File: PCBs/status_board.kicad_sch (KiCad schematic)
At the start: 19 parts, among them J1 Conn_01x03, J2 Conn_01x03, J3 Conn_01x02, J4 Conn_01x04, J5 Conn_01x04, J6 Conn_01x02, U1 XIAO-ESP32-S3-SMD

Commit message: Flipped voltage readout
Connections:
- net GND: now also J5.1 (Pin_1); no longer J5.4 (Pin_4)
- net at J1.3 (Pin_3), J2.3 (Pin_3), J4.3 (Pin_3)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: now also J5.2 (Pin_2); no longer J5.3 (Pin_3)
- net at U1.11 (D10): now also J5.3 (Pin_3); no longer J5.1 (Pin_1)
- net at U1.10 (D9): now also J5.4 (Pin_4); no longer J5.2 (Pin_2)
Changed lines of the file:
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@@
-	)
-	(junction
-		(at 157.48 107.95)
-		(diameter 0)
-		(color 0 0 0 0)
 	)
 	(junction
@@
 		(color 0 0 0 0)
 	)
+	(junction
+		(at 166.37 99.06)
+		(diameter 0)
+		(color 0 0 0 0)
+	)
 	(wire
 		(pts
@@
 	(wire
 		(pts
-			(xy 166.37 102.87) (xy 167.64 102.87)
-		)
-		(stroke
-			(width 0)
-			(type default)
-		)
-	)
-	(wire
-		(pts
 			(xy 116.84 107.95) (xy 128.27 107.95)
 		)
@@
 	(wire
 		(pts
-			(xy 171.45 99.06) (xy 184.15 99.06)
-		)
-		(stroke
-			(width 0)
-			(type default)
-		)
-	)
-	(wire
-		(pts
 			(xy 46.99 64.77) (xy 46.99 68.58)
 		)
@@
 	(wire
 		(pts
-			(xy 175.26 104.14) (xy 171.45 107.95)
-		)
-		(stroke
-			(width 0)
-			(type default)
-		)
-	)
-	(wire
-		(pts
-			(xy 157.48 107.95) (xy 171.45 107.95)
-		)
-		(stroke
-			(width 0)
-			(type default)
-		)
-	)
-	(wire
-		(pts
 			(xy 59.69 57.15) (xy 92.71 57.15)
 		)
@@
 	(wire
 		(pts
+			(xy 167.64 104.14) (xy 166.37 102.87)
+		)
+		(stroke
+			(width 0)
+			(type default)
+		)
+	)
+	(wire
+		(pts
 			(xy 128.27 107.95) (xy 128.27 111.76)
 		)
@@
 	(wire
 		(pts
-			(xy 166.37 106.68) (xy 168.91 106.68)
-		)
-		(stroke
-			(width 0)
-			(type default)
-		)
-	)
-	(wire
-		(pts
 			(xy 109.22 111.76) (xy 109.22 110.49)
 		)
@@
 	(wire
 		(pts
+			(xy 184.15 101.6) (xy 168.91 101.6)
+		)
+		(stroke
+			(width 0)
+			(type default)
+		)
+	)
+	(wire
+		(pts
 			(xy 83.82 64.77) (xy 83.82 67.31)
 		)
@@
 	(wire
 		(pts
+			(xy 166.37 106.68) (xy 184.15 106.68)
+		)
+		(stroke
+			(width 0)
+			(type default)
+		)
+	)
+	(wire
+		(pts
 			(xy 72.39 64.77) (xy 72.39 71.12)
 		)
@@
 	(wire
 		(pts
-			(xy 173.99 101.6) (xy 184.15 101.6)
-		)
-		(stroke
-			(width 0)
-			(type default)
-		)
-	)
-	(wire
-		(pts
-			(xy 168.91 106.68) (xy 173.99 101.6)
-		)
-		(stroke
-			(width 0)
-			(type default)
-		)
-	)
-	(wire
-		(pts
 			(xy 96.52 64.77) (xy 96.52 68.58)
 		)
@@
 	(wire
 		(pts
-			(xy 167.64 102.87) (xy 171.45 99.06)
+			(xy 168.91 101.6) (xy 166.37 99.06)
 		)
 		(stroke
@@
 	(wire
 		(pts
-			(xy 175.26 104.14) (xy 184.15 104.14)
+			(xy 184.15 104.14) (xy 167.64 104.14)
 		)
 		(stroke
@@
 	(symbol
 		(lib_id "power:GND")
-		(at 184.15 106.68 270)
+		(at 184.15 99.06 270)
 		(unit 1)
 		(body_style 1)
@@
 		(fields_autoplaced yes)
 		(property "Reference" "#PWR07"
-			(at 177.8 106.68 0)
+			(at 177.8 99.06 0)
 			(hide yes)
 			(show_name no)
@@
 		)
 		(property "Value" "GND"
-			(at 180.34 106.6799 90)
+			(at 180.34 99.0599 90)
 			(show_name no)
 			(do_not_autoplace no)
@@
 		)
 		(property "Footprint" ""
-			(at 184.15 106.68 0)
+			(at 184.15 99.06 0)
 			(hide yes)
 			(show_name no)
@@
 		)
 		(property "Datasheet" ""
-			(at 184.15 106.68 0)
+			(at 184.15 99.06 0)
 			(hide yes)
 			(show_name no)
@@
 		)
 		(property "Description" "Power symbol creates a global label with name \"GND\" , ground"
-			(at 184.15 106.68 0)
-			(hide yes)
-			(show_name no)
+			(at 184.15 99.06 0)
+			(hide yes)
+			(show_name no)

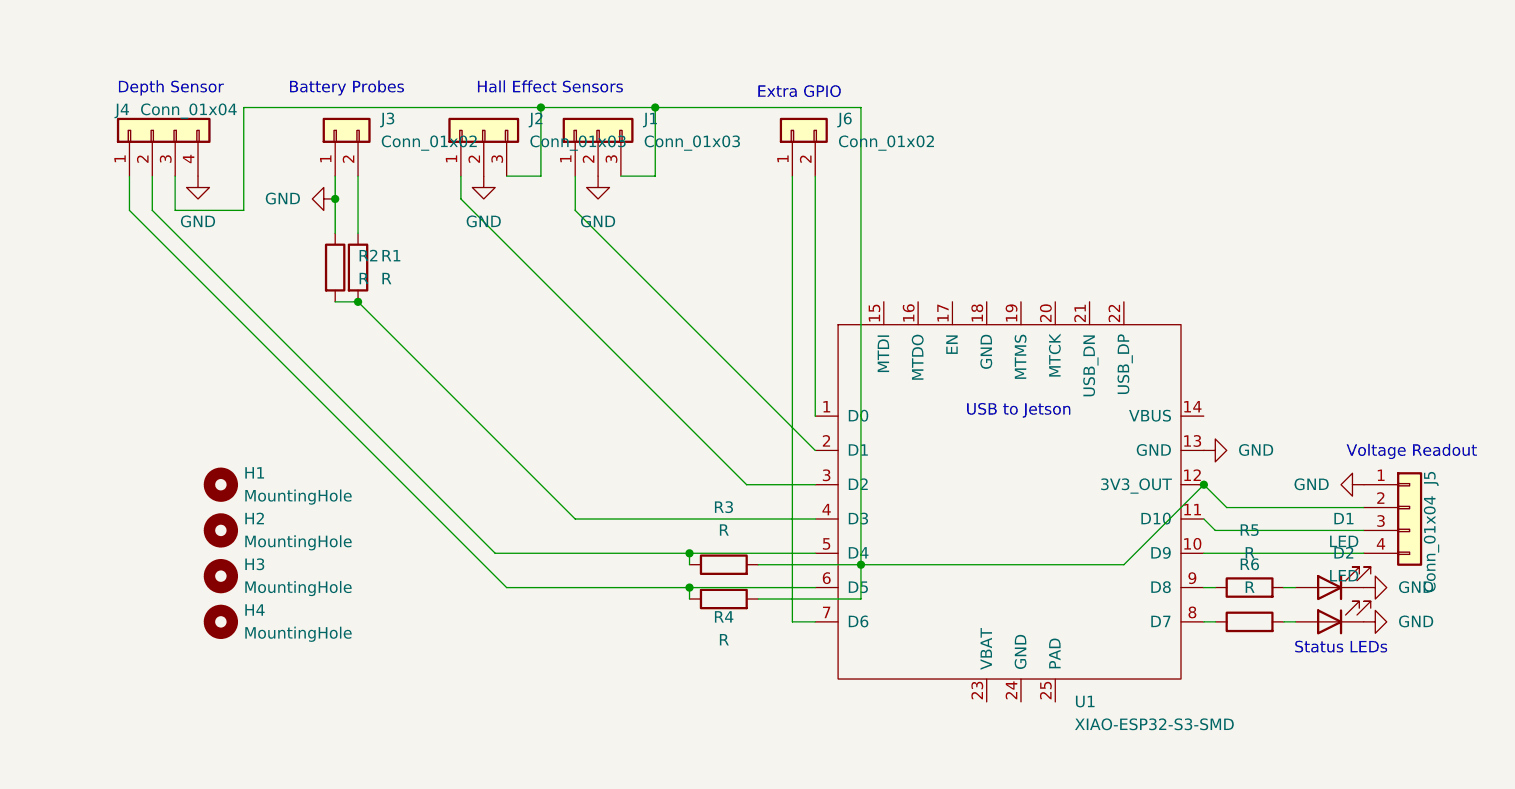
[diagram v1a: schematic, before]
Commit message: Removed connection crossover
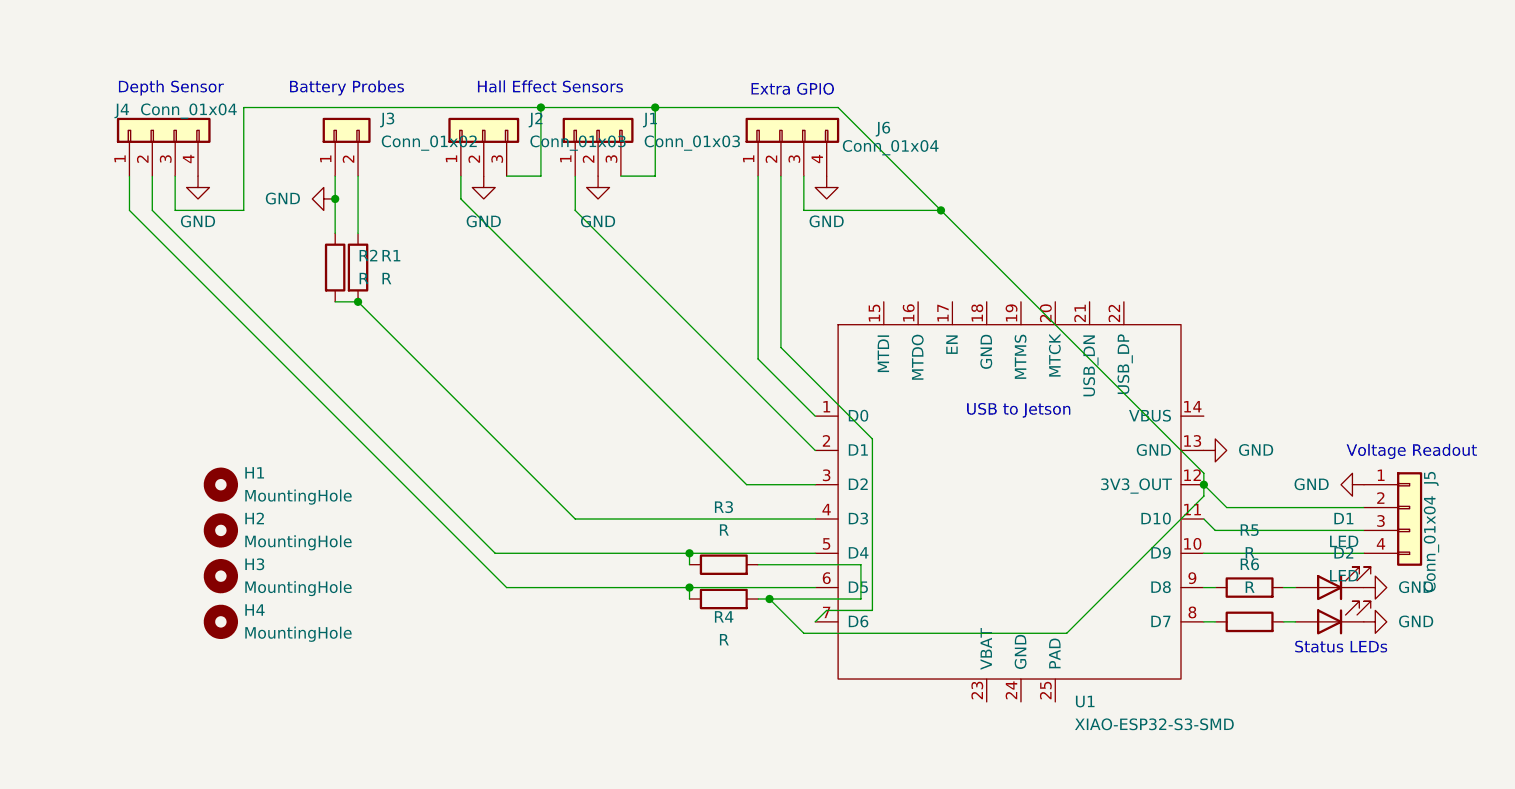
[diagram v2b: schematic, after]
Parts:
- removed J6: Conn_01x02, symbol Connector_Generic:Conn_01x02
- added J6: Conn_01x04, symbol Connector_Generic:Conn_01x04
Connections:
- net GND: now also J6.4 (Pin_4)
- net at J1.3 (Pin_3), J2.3 (Pin_3), J4.3 (Pin_3)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: now also J6.3 (Pin_3)
- net at U1.7 (D6): now also J6.2 (Pin_2)
- net at U1.1 (D0): now also J6.1 (Pin_1)

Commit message: Replace ESP32 sch with regular connectors
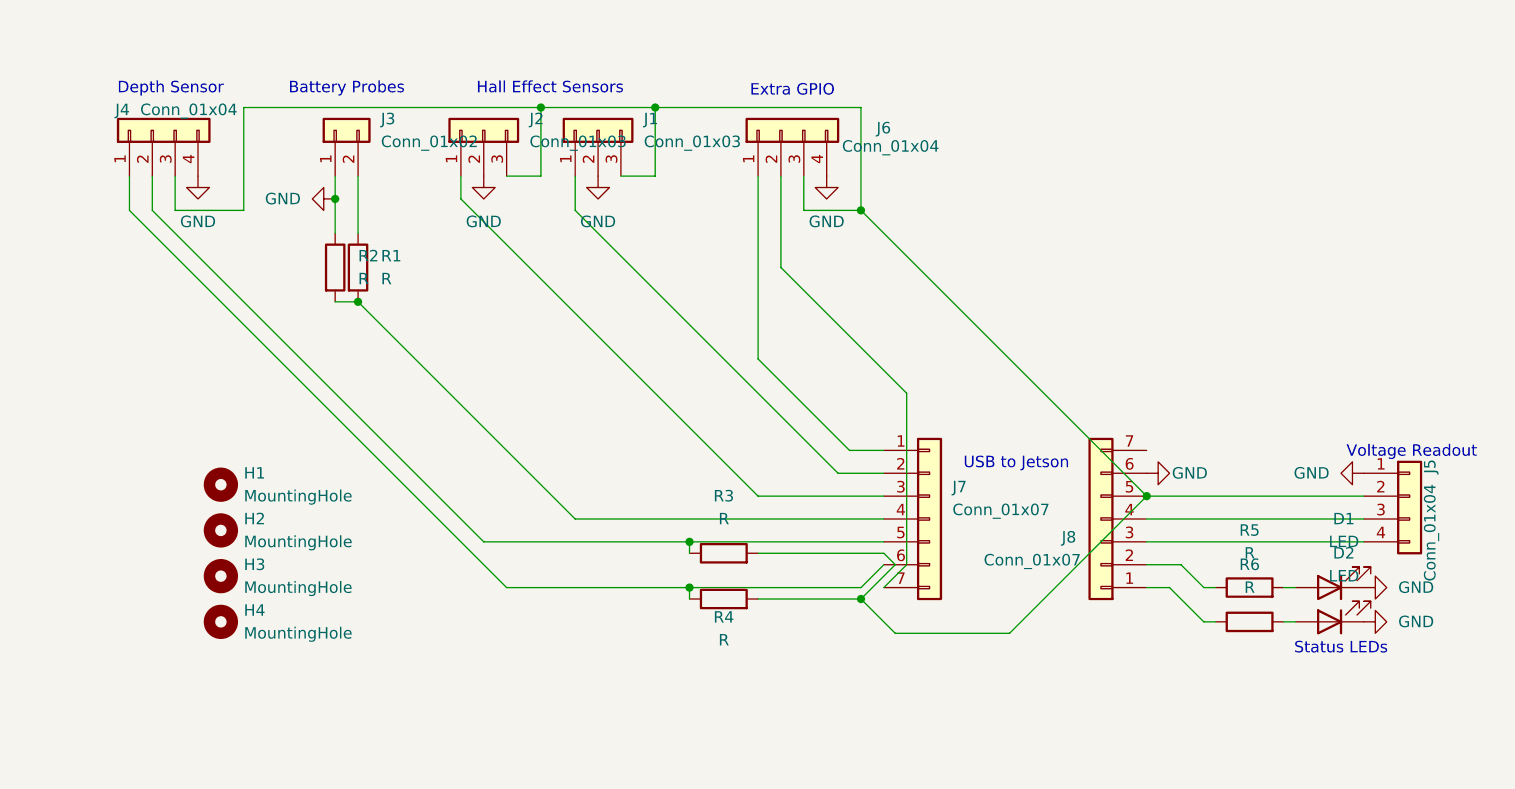
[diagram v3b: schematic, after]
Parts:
- removed U1: XIAO-ESP32-S3-SMD, Seeed_Studio_XIAO_Series:XIAO-ESP32-S3-SMD, symbol Seeed_Studio_XIAO_Series:XIAO-ESP32-S3-SMD
- added J7, J8: Conn_01x07, symbol Connector_Generic:Conn_01x07
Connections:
- net GND: now also J8.6 (Pin_6)
- net at R5.1: now also J8.2 (Pin_2)
- net at J4.1 (Pin_1), R4.1: now also J7.6 (Pin_6)
- net at J1.3 (Pin_3), J2.3 (Pin_3), J4.3 (Pin_3)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: now also J8.5 (Pin_5)
- net at J4.2 (Pin_2), R3.1: now also J7.5 (Pin_5)
- net at J2.1 (Pin_1): now also J7.3 (Pin_3)
- net at R6.1: now also J8.1 (Pin_1)
- net at R1.2, R2.2: now also J7.4 (Pin_4)
- net at J5.3 (Pin_3): now also J8.4 (Pin_4)
- net at J5.4 (Pin_4): now also J8.3 (Pin_3)
- net at J6.1 (Pin_1): now also J7.1 (Pin_1)
- net at J6.2 (Pin_2): now also J7.7 (Pin_7)
- net at J1.1 (Pin_1): now also J7.2 (Pin_2)
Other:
- moved on the sheet: J5, R3

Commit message: connector for each type of depth sens
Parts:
- added J9: Conn_01x04, symbol Connector_Generic:Conn_01x04
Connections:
- net GND: now also J9.4 (Pin_4)
- net at J4.1 (Pin_1), J7.6 (Pin_6), R4.1: now also J9.1 (Pin_1)
- net at J1.3 (Pin_3), J2.3 (Pin_3), J4.3 (Pin_3)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: now also J9.3 (Pin_3)
- net at J4.2 (Pin_2), J7.5 (Pin_5), R3.1: now also J9.2 (Pin_2)
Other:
- note added: "Depth Sensor (1x, 2x conn.)"
- note removed: "Depth Sensor"
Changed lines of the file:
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@@
 		)
 	)
-	(text "Depth Sensor\n"
-		(exclude_from_sim no)
-		(at 51.562 55.118 0)
+	(text "Depth Sensor (1x, 2x conn.)\n"
+		(exclude_from_sim no)
+		(at 51.054 48.768 0)
 		(effects
 			(font
@@
 	)
 	(junction
+		(at 49.53 64.77)
+		(diameter 0)
+		(color 0 0 0 0)
+	)
+	(junction
 		(at 109.22 110.49)
 		(diameter 0)
@@
 	)
 	(junction
+		(at 52.07 64.77)
+		(diameter 0)
+		(color 0 0 0 0)
+	)
+	(junction
 		(at 109.22 105.41)
 		(diameter 0)
@@
 	)
 	(junction
+		(at 54.61 64.77)
+		(diameter 0)
+		(color 0 0 0 0)
+	)
+	(junction
 		(at 69.85 67.31)
 		(diameter 0)
@@
 	)
 	(junction
+		(at 46.99 64.77)
+		(diameter 0)
+		(color 0 0 0 0)
+	)
+	(junction
 		(at 92.71 57.15)
 		(diameter 0)
@@
 	(wire
 		(pts
+			(xy 50.8 63.5) (xy 50.8 59.69)
+		)
+		(stroke
+			(width 0)
+			(type default)
+		)
+	)
+	(wire
+		(pts
 			(xy 88.9 110.49) (xy 109.22 110.49)
 		)
@@
 	(wire
 		(pts
+			(xy 49.53 64.77) (xy 50.8 63.5)
+		)
+		(stroke
+			(width 0)
+			(type default)
+		)
+	)
+	(wire
+		(pts
 			(xy 166.37 110.49) (xy 167.64 110.49)
 		)
@@
 	(wire
 		(pts
+			(xy 50.8 59.69) (xy 49.53 58.42)
+		)
+		(stroke
+			(width 0)
+			(type default)
+		)
+	)
+	(wire
+		(pts
 			(xy 109.22 111.76) (xy 109.22 110.49)
 		)
@@
 	(wire
 		(pts
+			(xy 46.99 64.77) (xy 48.26 63.5)
+		)
+		(stroke
+			(width 0)
+			(type default)
+		)
+	)
+	(wire
+		(pts
 			(xy 72.39 64.77) (xy 72.39 71.12)
 		)
@@
 	(wire
 		(pts
+			(xy 54.61 64.77) (xy 55.88 63.5)
+		)
+		(stroke
+			(width 0)
+			(type default)
+		)
+	)
+	(wire
+		(pts
 			(xy 96.52 64.77) (xy 96.52 68.58)
 		)
@@
 	(wire
 		(pts
+			(xy 48.26 63.5) (xy 48.26 59.69)
+		)
+		(stroke
+			(width 0)
+			(type default)
+		)
+	)
+	(wire
+		(pts
 			(xy 52.07 68.58) (xy 59.69 68.58)
 		)
@@
 	(wire
 		(pts
+			(xy 53.34 59.69) (xy 52.07 58.42)
+		)
+		(stroke
+			(width 0)
+			(type default)
+		)
+	)
+	(wire
+		(pts
 			(xy 133.35 88.9) (xy 133.35 107.95)
 		)
@@
 	(wire
 		(pts
+			(xy 48.26 59.69) (xy 46.99 58.42)
+		)
+		(stroke
+			(width 0)
+			(type default)
+		)
+	)
+	(wire
+		(pts
 			(xy 119.38 64.77) (xy 119.38 74.93)
 		)
@@
 	(wire
 		(pts
+			(xy 53.34 59.69) (xy 53.34 63.5)
+		)
+		(stroke
+			(width 0)
+			(type default)
+		)
+	)
+	(wire
+		(pts
 			(xy 160.02 100.33) (xy 184.15 100.33)
 		)
@@
 	(wire
 		(pts
+			(xy 55.88 59.69) (xy 54.61 58.42)
+		)
+		(stroke
+			(width 0)
+			(type default)
+		)
+	)
+	(wire
+		(pts
 			(xy 92.71 57.15) (xy 105.41 57.15)
 		)
@@
 	(wire
 		(pts
+			(xy 52.07 64.77) (xy 53.34 63.5)
+		)
+		(stroke
+			(width 0)
+			(type default)
+		)
+	)
+	(wire
+		(pts
 			(xy 128.27 57.15) (xy 128.27 68.58)
+		)
+		(stroke
+			(width 0)
+			(type default)
+		)
+	)
+	(wire
+		(pts
+			(xy 55.88 63.5) (xy 55.88 59.69)
 		)
 		(stroke
@@
 					(unit 1)
 				)
+			)
+		)
+	)
+	(symbol
+		(lib_id "Connector_Generic:Conn_01x04")
+		(at 49.53 53.34 90)
+		(unit 1)
+		(body_style 1)
+		(exclude_from_sim no)
+		(in_bom yes)
+		(on_board yes)
+		(in_pos_files yes)
+		(dnp no)
+		(property "Reference" "J9"
+			(at 46.228 51.054 90)
+			(show_name no)
+			(do_not_autoplace no)
+			(effects
+				(font
+					(size 1.27 1.27)
+				)
+			)
+		)
+		(property "Value" "Conn_01x04"
+			(at 53.594 51.054 90)
+			(show_name no)
+			(do_not_autoplace no)
+			(effects
+				(font
+					(size 1.27 1.27)
+				)
+			)
+		)
+		(property "Footprint" ""
+			(at 49.53 53.34 0)
+			(hide yes)
+			(show_name no)
+			(do_not_autoplace no)
+			(effects
+				(font
+					(size 1.27 1.27)
+				)
+			)
+		)
+		(property "Datasheet" ""
+			(at 49.53 53.34 0)
+			(hide yes)
+			(show_name no)
+			(do_not_autoplace no)
+			(effects
+				(font
+					(size 1.27 1.27)
+				)
+			)
+		)
+		(property "Description" "Generic connector, single row, 01x04, script generated (kicad-library-utils/schlib/autogen/connector/)"
+			(at 49.53 53.34 0)
+			(hide yes)
+			(show_name no)
+			(do_not_autoplace no)
+			(effects
+				(font
+					(size 1.27 1.27)
+				)
+			)
+		)
+		(pin "1"
+		)
+		(pin "2"
+		)
+		(pin "3"
+		)
+		(pin "4"
+		)
+		(instances
+			(project "status_board"
+				(path "/4c986fa9-a957-4ae2-82f6-4f95104bacdd"
+					(reference "J9")
+					(unit 1)
+				)

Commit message: Adjust depth sens. wiring order
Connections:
- net at J7.6 (Pin_6), R4.1: now also J4.2 (Pin_2), J9.2 (Pin_2); no longer J4.1 (Pin_1), J9.1 (Pin_1)
- net at J1.3 (Pin_3), J2.3 (Pin_3), J5.2 (Pin_2)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: now also J4.1 (Pin_1), J9.1 (Pin_1); no longer J4.3 (Pin_3), J9.3 (Pin_3)
- net at J7.5 (Pin_5), R3.1: now also J4.3 (Pin_3), J9.3 (Pin_3); no longer J4.2 (Pin_2), J9.2 (Pin_2)
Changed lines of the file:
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@@
+	)
+	(junction
+		(at 109.22 105.41)
+		(diameter 0)
+		(color 0 0 0 0)
+	)
+	(junction
+		(at 72.39 78.74)
+		(diameter 0)
+		(color 0 0 0 0)
+	)
+	(junction
+		(at 54.61 64.77)
+		(diameter 0)
+		(color 0 0 0 0)
+	)
+	(junction
+		(at 69.85 67.31)
+		(diameter 0)
+		(color 0 0 0 0)
 	)
 	(junction
@@
 	)
 	(junction
-		(at 109.22 105.41)
-		(diameter 0)
-		(color 0 0 0 0)
-	)
-	(junction
-		(at 72.39 78.74)
-		(diameter 0)
-		(color 0 0 0 0)
-	)
-	(junction
-		(at 54.61 64.77)
-		(diameter 0)
-		(color 0 0 0 0)
-	)
-	(junction
-		(at 69.85 67.31)
-		(diameter 0)
-		(color 0 0 0 0)
-	)
-	(junction
 		(at 160.02 100.33)
 		(diameter 0)
@@
 	(wire
 		(pts
+			(xy 44.45 50.8) (xy 55.88 50.8)
+		)
+		(stroke
+			(width 0)
+			(type default)
+		)
+	)
+	(wire
+		(pts
 			(xy 163.83 107.95) (xy 166.37 110.49)
 		)
@@
 	(wire
 		(pts
-			(xy 88.9 110.49) (xy 109.22 110.49)
-		)
-		(stroke
-			(width 0)
-			(type default)
-		)
-	)
-	(wire
-		(pts
 			(xy 101.6 64.77) (xy 105.41 64.77)
 		)
@@
 	(wire
 		(pts
-			(xy 46.99 64.77) (xy 46.99 68.58)
+			(xy 62.23 57.15) (xy 92.71 57.15)
 		)
 		(stroke
@@
 	(wire
 		(pts
-			(xy 46.99 68.58) (xy 88.9 110.49)
-		)
-		(stroke
-			(width 0)
-			(type default)
-		)
-	)
-	(wire
-		(pts
 			(xy 69.85 78.74) (xy 72.39 78.74)
 		)
@@
 	(wire
 		(pts
-			(xy 49.53 64.77) (xy 49.53 68.58)
-		)
-		(stroke
-			(width 0)
-			(type default)
-		)
-	)
-	(wire
-		(pts
 			(xy 96.52 102.87) (xy 72.39 78.74)
 		)
@@
 	(wire
 		(pts
-			(xy 59.69 57.15) (xy 92.71 57.15)
+			(xy 44.45 62.23) (xy 46.99 64.77)
 		)
 		(stroke
@@
 	(wire
 		(pts
+			(xy 86.36 110.49) (xy 109.22 110.49)
+		)
+		(stroke
+			(width 0)
+			(type default)
+		)
+	)
+	(wire
+		(pts
 			(xy 54.61 64.77) (xy 55.88 63.5)
 		)
@@
 	(wire
 		(pts
+			(xy 52.07 64.77) (xy 52.07 71.12)
+		)
+		(stroke
+			(width 0)
+			(type default)
+		)
+	)
+	(wire
+		(pts
 			(xy 128.27 111.76) (xy 132.08 115.57)
 		)
@@
 	(wire
 		(pts
-			(xy 59.69 57.15) (xy 59.69 68.58)
-		)
-		(stroke
-			(width 0)
-			(type default)
-		)
-	)
-	(wire
-		(pts
-			(xy 49.53 68.58) (xy 86.36 105.41)
-		)
-		(stroke
-			(width 0)
-			(type default)
-		)
-	)
-	(wire
-		(pts
 			(xy 88.9 64.77) (xy 92.71 64.77)
 		)
@@
 	(wire
 		(pts
-			(xy 52.07 68.58) (xy 59.69 68.58)
+			(xy 49.53 73.66) (xy 86.36 110.49)
+		)
+		(stroke
+			(width 0)
+			(type default)
+		)
+	)
+	(wire
+		(pts
+			(xy 44.45 50.8) (xy 44.45 62.23)
 		)
 		(stroke
@@
 	(wire
 		(pts
+			(xy 52.07 71.12) (xy 86.36 105.41)
+		)
+		(stroke
+			(width 0)
+			(type default)
+		)
+	)
+	(wire
+		(pts
 			(xy 53.34 59.69) (xy 52.07 58.42)
 		)
@@
 	(wire
 		(pts
-			(xy 52.07 64.77) (xy 52.07 68.58)
-		)
-		(stroke
-			(width 0)
-			(type default)
-		)
-	)
-	(wire
-		(pts
 			(xy 166.37 114.3) (xy 167.64 114.3)
 		)
@@
 	(wire
 		(pts
+			(xy 49.53 64.77) (xy 49.53 73.66)
+		)
+		(stroke
+			(width 0)
+			(type default)
+		)
+	)
+	(wire
+		(pts
 			(xy 92.71 57.15) (xy 105.41 57.15)
 		)
@@
 		)
 		(stroke
+			(width 0)
+			(type default)
+		)
+	)
+	(wire
+		(pts
+			(xy 62.23 57.15) (xy 55.88 50.8)
+		)
+		(stroke
